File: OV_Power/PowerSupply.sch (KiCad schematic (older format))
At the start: 16 parts, among them J1 Kycon_kpjx-4s_shielded, J2 Conn_HDR_2x10_latching, J3 532530670, J6 CONN_HEADER_2.54X2_MOLEX_KK_S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, J7 CONN_HEADER_2.54X2_MOLEX_KK_S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, Q3 SZNUD3124LT1G, Q4 SZNUD3124LT1G, U7 LTC4416, U8 AOSD21307, U9 AOSD21307

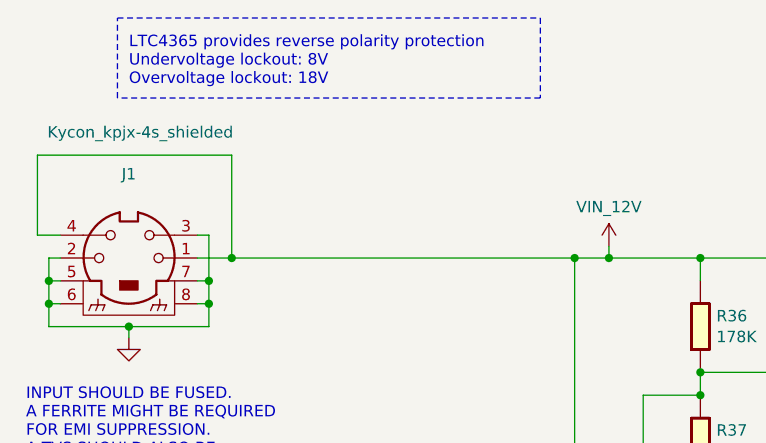
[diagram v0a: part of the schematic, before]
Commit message: 12V power supply vendor changed.  Of course the pinouts for the power connector are different, argh...
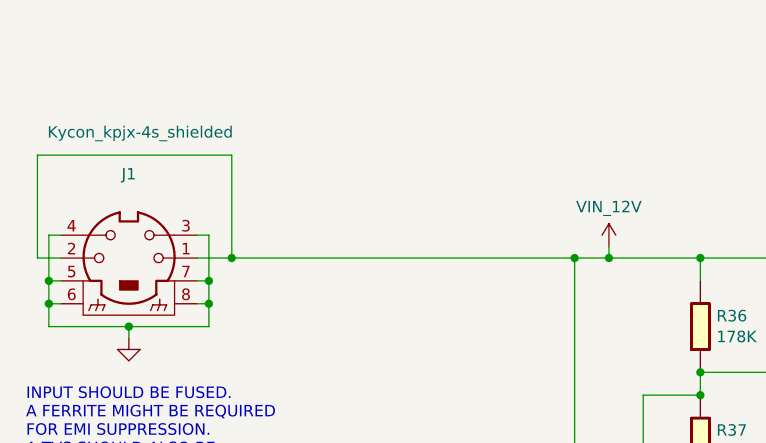
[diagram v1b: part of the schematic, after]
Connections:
- net GND: now also J1.4; no longer J1.2
- net VIN_12V: now also J1.2; no longer J1.4
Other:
- note removed: "LTC4365 provides reverse polarity protection\nUndervoltage lockout: 8V\nOvervoltage lockout: 18V"
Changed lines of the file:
@@
 	1    0    0    -1
 $EndComp
-Text Notes 1050 950  0    50   ~ 0
-LTC4365 provides reverse polarity protection\nUndervoltage lockout: 8V\nOvervoltage lockout: 18V
-Wire Notes Line
-	1000 650  2850 650
-Wire Notes Line
-	2850 650  2850 1000
-Wire Notes Line
-	2850 1000 1000 1000
-Wire Notes Line
-	1000 1000 1000 650
 $Comp
 L OV_Power-rescue:LTC4416-OpenVent U7
@@
 $EndComp
 Wire Wire Line
-	750  1600 650  1600
-Wire Wire Line
-	650  1600 650  1250
-Wire Wire Line
 	650  1250 1500 1250
 Wire Wire Line
@@
 Wire Wire Line
 	700  2000 700  1900
-Wire Wire Line
-	700  1700 750  1700
 Wire Wire Line
 	1050 2000 1050 2050
@@
 Wire Wire Line
 	750  1800 700  1800
-Connection ~ 700  1800
-Wire Wire Line
-	700  1800 700  1700
 Wire Wire Line
 	750  1900 700  1900
@@
 Wire Wire Line
 	3000 1700 3150 1700
+Wire Wire Line
+	750  1700 650  1700
+Wire Wire Line
+	650  1700 650  1250
+Wire Wire Line
+	750  1600 700  1600
+Wire Wire Line
+	700  1600 700  1800
+Connection ~ 700  1800
 $EndSCHEMATC

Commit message: Minor documentation change.
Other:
- note added: "Switch 1"
- note added: "Switch 2"
- note added: "Switch 3"
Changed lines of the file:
@@
 U 1 1 5FC7E477
 P 4200 6600
-F 0 "J3" H 4280 6592 50  0000 L CNN
-F 1 "532530670" H 4280 6501 50  0000 L CNN
+F 0 "J3" H 4150 6950 50  0000 L CNN
+F 1 "532530670" H 4000 6200 50  0000 L CNN
 F 2 "Connector_Molex:Molex_Micro-Latch_53253-0670_1x06_P2.00mm_Vertical" H 4200 6600 50  0001 C CNN
 F 3 "https://www.molex.com/pdm_docs/sd/532530270_sd.pdf" H 4200 6600 50  0001 C CNN
@@
 	700  1600 700  1800
 Connection ~ 700  1800
+Text Notes 4300 6400 0    50   ~ 0
+Switch 3
+Text Notes 4300 6500 0    50   ~ 0
+Switch 2
+Text Notes 4300 6600 0    50   ~ 0
+Switch 1
 $EndSCHEMATC

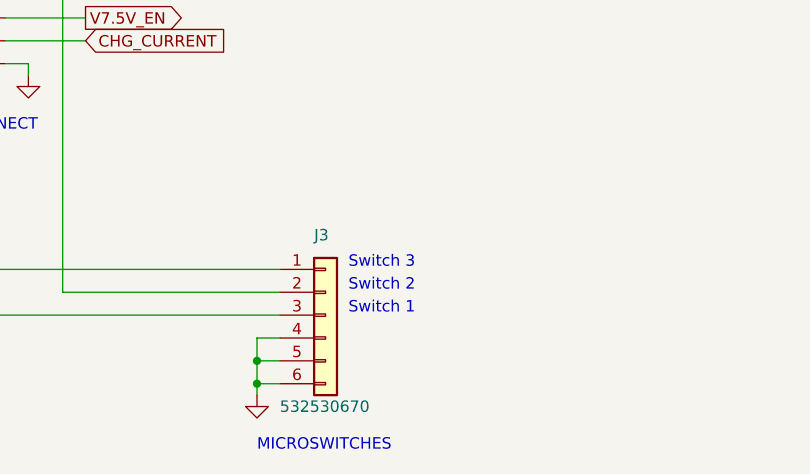
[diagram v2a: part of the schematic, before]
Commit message: Some naming changes to microswitch signals requested by Laura.
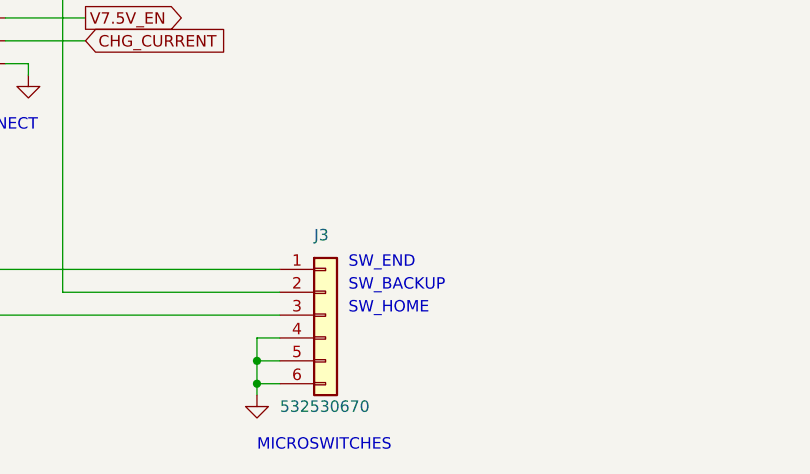
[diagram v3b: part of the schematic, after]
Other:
- note added: "SW_BACKUP"
- note added: "SW_END"
- note added: "SW_HOME"
- note removed: "Switch 1"
- note removed: "Switch 2"
- note removed: "Switch 3"
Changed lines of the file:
@@
 Connection ~ 700  1800
 Text Notes 4300 6400 0    50   ~ 0
-Switch 3
+SW_END
 Text Notes 4300 6500 0    50   ~ 0
-Switch 2
+SW_BACKUP
 Text Notes 4300 6600 0    50   ~ 0
-Switch 1
+SW_HOME
 $EndSCHEMATC

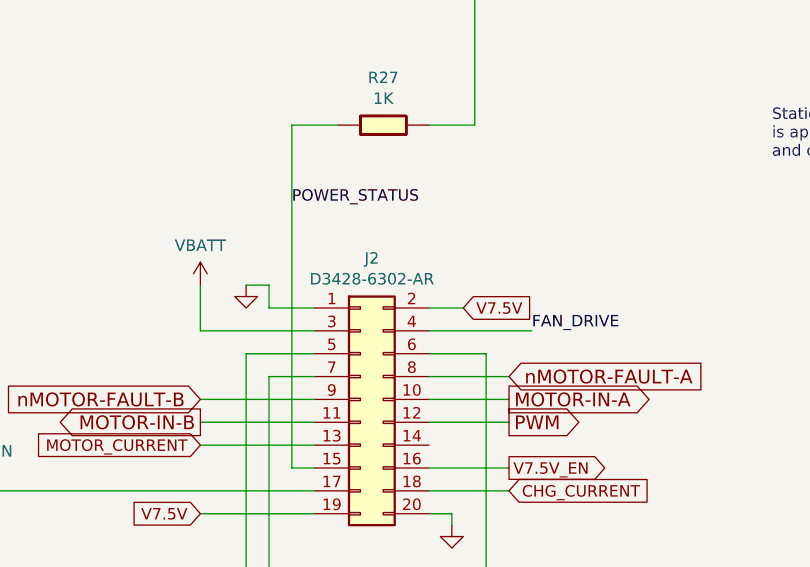
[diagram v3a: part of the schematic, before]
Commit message: Current limiting on regulators and pin swapping between power and main board
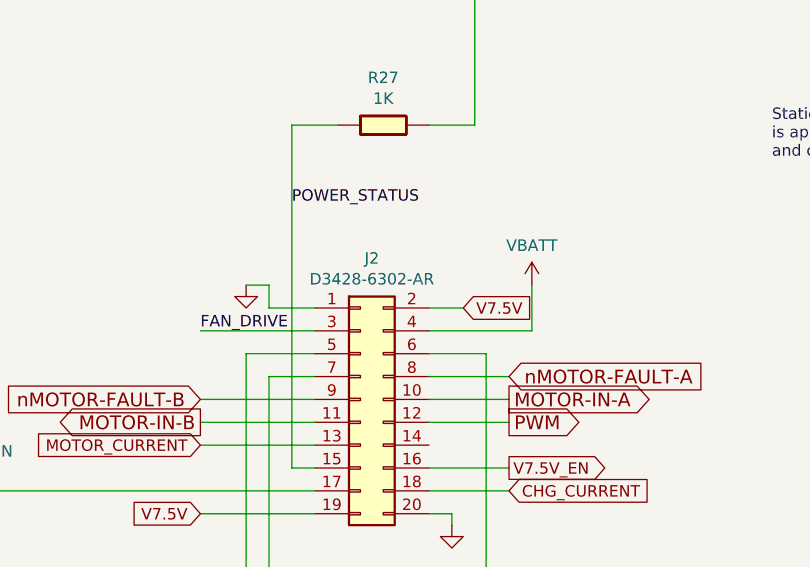
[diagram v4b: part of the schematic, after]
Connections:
- net FAN_DRIVE: now also J2.3 (Pin_3); no longer J2.4 (Pin_4)
- net VBATT: now also J2.4 (Pin_4); no longer J2.3 (Pin_3)
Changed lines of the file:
@@
 L OV_Power-rescue:VBATT-OpenVent #PWR032
 U 1 1 5FB6E37F
-P 1800 4500
-F 0 "#PWR032" H 1800 4350 50  0001 C CNN
-F 1 "VBATT" H 1800 4673 50  0000 C CNN
-F 2 "" H 1800 4500 50  0001 C CNN
-F 3 "" H 1800 4500 50  0001 C CNN
-	1    1800 4500
-	1    0    0    -1
-$EndComp
-Wire Wire Line
-	1800 4700 1800 4500
+P 3250 4500
+F 0 "#PWR032" H 3250 4350 50  0001 C CNN
+F 1 "VBATT" H 3250 4673 50  0000 C CNN
+F 2 "" H 3250 4500 50  0001 C CNN
+F 3 "" H 3250 4500 50  0001 C CNN
+	1    3250 4500
+	1    0    0    -1
+$EndComp
+Wire Wire Line
+	3250 4700 3250 4500
 Text GLabel 3150 5100 2    60   Output ~ 0
 PWM
@@
 Wire Wire Line
 	8650 4800 8750 4800
-Text Label 3250 4700 0    50   ~ 0
+Text Label 1800 4700 0    50   ~ 0
 FAN_DRIVE
 Wire Wire Line

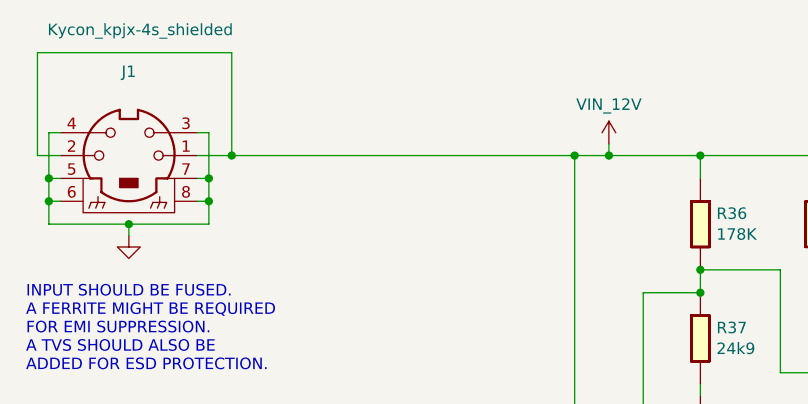
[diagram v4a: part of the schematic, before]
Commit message: Update PowerSupply.sch
Fuse added to main supply
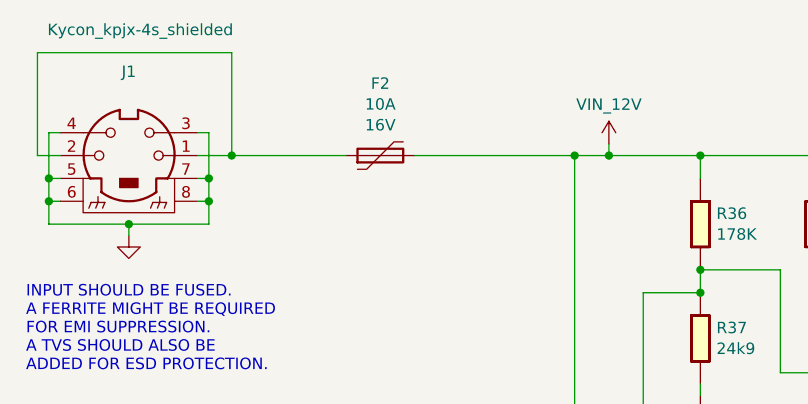
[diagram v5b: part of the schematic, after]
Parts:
- added F2: Polyfuse_10A-OpenVent, symbol OV_Power-rescue:Polyfuse_10A-OpenVent
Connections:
- net VIN_12V: now also F2.2; no longer J1.1, J1.2
- new net: F2.1, J1.1, J1.2
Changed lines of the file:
@@
 Text Label 8200 5300 2    50   ~ 0
 FAN_DRIVE
-Wire Wire Line
-	1500 1700 3000 1700
-Connection ~ 1500 1700
 Connection ~ 3550 1700
 $Comp
@@
 Wire Wire Line
 	3000 3800 3000 1700
-Connection ~ 3000 1700
 Wire Wire Line
 	3000 1700 3150 1700
@@
 Text Notes 4300 6600 0    50   ~ 0
 SW_HOME
+$Comp
+L OV_Power-rescue:Polyfuse_10A-OpenVent F2
+U 1 1 60ED2B74
+P 2150 1700
+F 0 "F2" V 2465 1700 50  0000 C CNN
+F 1 "Polyfuse_10A-OpenVent" V 2250 1700 50  0001 C CNN
+F 2 "" H 2200 1500 50  0001 L CNN
+F 3 "" H 2150 1700 50  0001 C CNN
+F 4 "Littelfuse Inc." H 2150 1700 50  0001 C CNN "Mfr"
+F 5 "16R1000GMR" H 2150 1700 50  0001 C CNN "Mfr_PN"
+F 6 "PTC RESET FUSE 16V 10A RADIAL" H 2150 1700 50  0001 C CNN "Desc"
+F 7 "Polymeric PTC Resettable Fuse 16V 10A Ih Through Hole Radial, Disc" H 2150 1700 50  0001 C CNN "Detailed"
+F 8 "10A" V 2374 1700 50  0000 C CNN "Current"
+F 9 "16V" V 2283 1700 50  0000 C CNN "Voltage"
+	1    2150 1700
+	0    -1   -1   0
+$EndComp
+Wire Wire Line
+	2300 1700 3000 1700
+Connection ~ 3000 1700
+Wire Wire Line
+	2000 1700 1500 1700
+Connection ~ 1500 1700
 $EndSCHEMATC
